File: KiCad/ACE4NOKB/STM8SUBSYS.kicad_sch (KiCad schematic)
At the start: 6 parts, among them J400 614008235023, J402 Conn_02x05_Odd_Even, J403 STLink2, J408 Conn_02x05_Odd_Even

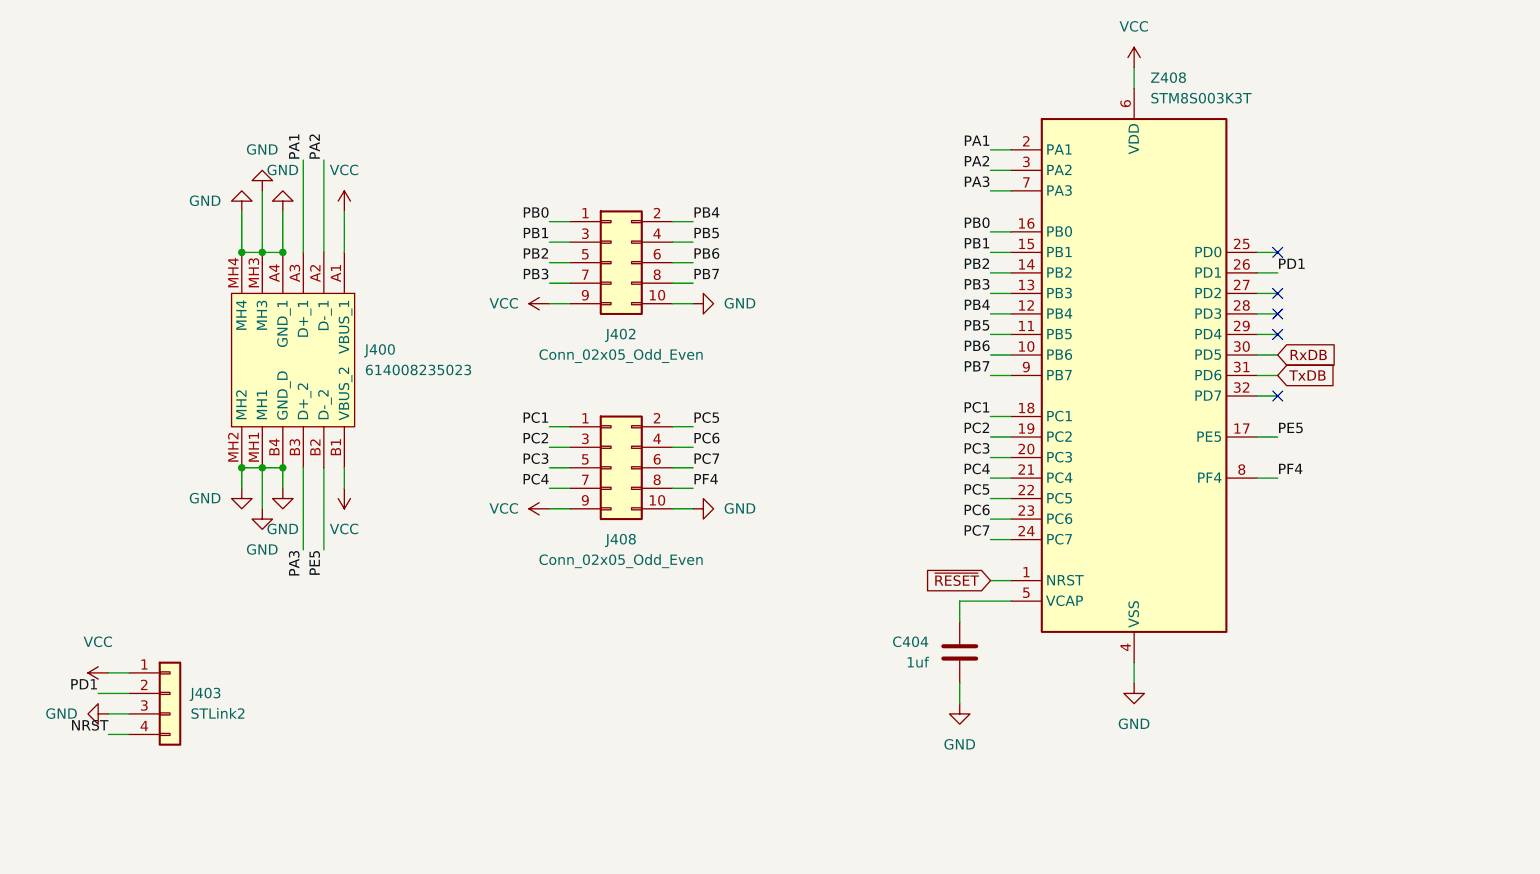
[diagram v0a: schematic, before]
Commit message: Fix mistake with ROM Select.
Signed-off-by: John Bradley <flypie@rocketmail.com>
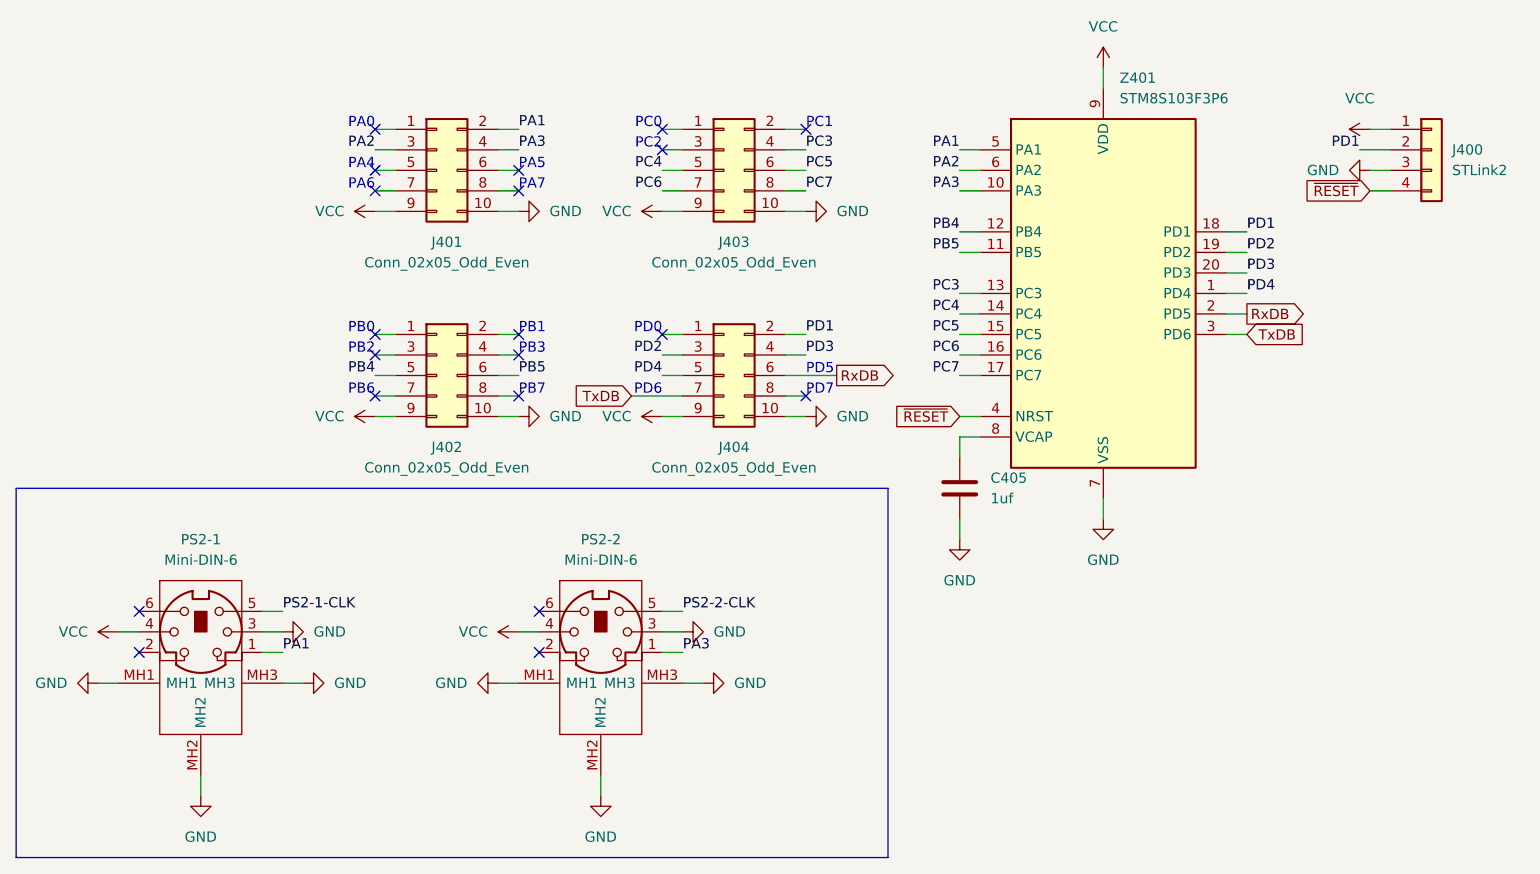
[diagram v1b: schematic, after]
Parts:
- removed C404: 1uf, Capacitor_THT:C_Disc_D3.0mm_W1.6mm_P2.50mm, symbol Device:C
- removed J400: 614008235023, 614008235023, symbol ExtraSymbols:614008235023
- removed J403: STLink2, Connector_PinHeader_2.54mm:PinHeader_1x04_P2.54mm_Vertical, symbol Connector_Generic:Conn_01x04
- removed J408: Conn_02x05_Odd_Even, Connector_PinHeader_2.54mm:PinHeader_2x05_P2.54mm_Vertical, symbol Connector_Generic:Conn_02x05_Odd_Even
- removed Z408: STM8S003K3T, Package_QFP:LQFP-32_7x7mm_P0.8mm, symbol MCU_ST_STM8:STM8S003K3T
- added C405: 1uf, Capacitor_THT:C_Disc_D3.0mm_W1.6mm_P2.50mm, symbol Device:C
- added J400: STLink2, Connector_PinHeader_2.54mm:PinHeader_1x04_P2.54mm_Vertical, symbol Connector_Generic:Conn_01x04
- added J401, J403, J404: Conn_02x05_Odd_Even, Connector_PinHeader_2.54mm:PinHeader_2x05_P2.54mm_Vertical, symbol Connector_Generic:Conn_02x05_Odd_Even
- added PS2-1, PS2-2: Mini-DIN-6, 57492661, symbol ExtraSymbols:5749266-1
- added Z401: STM8S103F3P6, Package_SO:TSSOP-20_4.4x6.5mm_P0.65mm, symbol MCU_ST_STM8:STM8S003F3P
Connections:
- net PB2 is gone; now on net PB4: J402.5 (Pin_5)
- net PB6 is gone; now on net PB5: J402.6 (Pin_6)
- net GND: now also C405.2, J400.3 (Pin_3), J401.10 (Pin_10), J403.10 (Pin_10), J404.10 (Pin_10), PS2-1.3, PS2-1.MH1, PS2-1.MH2, PS2-1.MH3, PS2-2.3, PS2-2.MH1, PS2-2.MH2, PS2-2.MH3, Z401.7 (VSS)
- net PA1: now also J401.2 (Pin_2), PS2-1.1, Z401.5 (PA1)
- net PA2: now also J401.3 (Pin_3), Z401.6 (PA2)
- net PA3: now also J401.4 (Pin_4), PS2-2.1, Z401.10 (PA3)
- net PB4: now also Z401.12 (PB4); no longer J402.2 (Pin_2)
- net PB5: now also Z401.11 (PB5); no longer J402.4 (Pin_4)
- net PC3: now also J403.4 (Pin_4), Z401.13 (PC3)
- net PC4: now also J403.5 (Pin_5), Z401.14 (PC4)
- net PC5: now also J403.6 (Pin_6), Z401.15 (PC5)
- net PC6: now also J403.7 (Pin_7), Z401.16 (PC6)
- net PC7: now also J403.8 (Pin_8), Z401.17 (PC7)
- net PD1: now also J400.2 (Pin_2), J404.2 (Pin_2), Z401.18 (PD1)
- net RxDB: now also J404.6 (Pin_6), Z401.2 (PD5)
- net TxDB: now also J404.7 (Pin_7), Z401.3 (PD6)
- net VCC: now also J400.1 (Pin_1), J401.9 (Pin_9), J403.9 (Pin_9), J404.9 (Pin_9), PS2-1.4, PS2-2.4, Z401.9 (VDD)
- net ~{RESET}: now also J400.4 (Pin_4), Z401.4 (NRST)
- net PB0: no longer names the net of J402.1 (Pin_1)
- net PB1: no longer names the net of J402.3 (Pin_3)
- net PB3: no longer names the net of J402.7 (Pin_7)
- net PB7: no longer names the net of J402.8 (Pin_8)
- new net: C405.1, Z401.8 (VCAP)
- new net PD2: J404.3 (Pin_3), Z401.19 (PD2)
- new net PD3: J404.4 (Pin_4), Z401.20 (PD3)
- new net PD4: J404.5 (Pin_5), Z401.1 (PD4)
- new net PS2-1-CLK: PS2-1.5
- new net PS2-2-CLK: PS2-2.5
- no-connect marks 5 -> 20
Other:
- note added: "PA0"
- note added: "PA4"
- note added: "PA5"
- note added: "PA6"
- note added: "PA7"
- note added: "PB0"
- note added: "PB1"
- note added: "PB2"
- note added: "PB3"
- note added: "PB6"
- note added: "PB7"
- note added: "PC0"
- note added: "PC1"
- note added: "PC2"
- note added: "PD0"
- note added: "PD5"
- note added: "PD6"
- note added: "PD7"
- title: ACE4NOKB -> JupiterAce Z80 plus KIO and new memory format.

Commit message: Update to last expermintal version. Uses clock sythsiser and can be switched between full ACE compatible and inhanced IO. Should be able to switch between multiple ROM images tosred on the same chip.
Signed-off-by: John Bradley <flypie@rocketmail.com>
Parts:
- C405: Manufacturer_Name Lelon -> (none); Manufacturer_Part_Number REA010M2CBK-0511P -> (none)
- J400: Manufacturer_Name Samtec -> (none); Manufacturer_Part_Number HTSW-104-24-F-S -> (none)
- J401, J402, J403, J404: Manufacturer_Name Amphenol FCI -> (none); Manufacturer_Part_Number 10129381-910001BLF -> (none)
- Z401: Manufacturer_Name STMicroelectronics -> (none); Manufacturer_Part_Number STM8S003K3T6CTR -> (none)

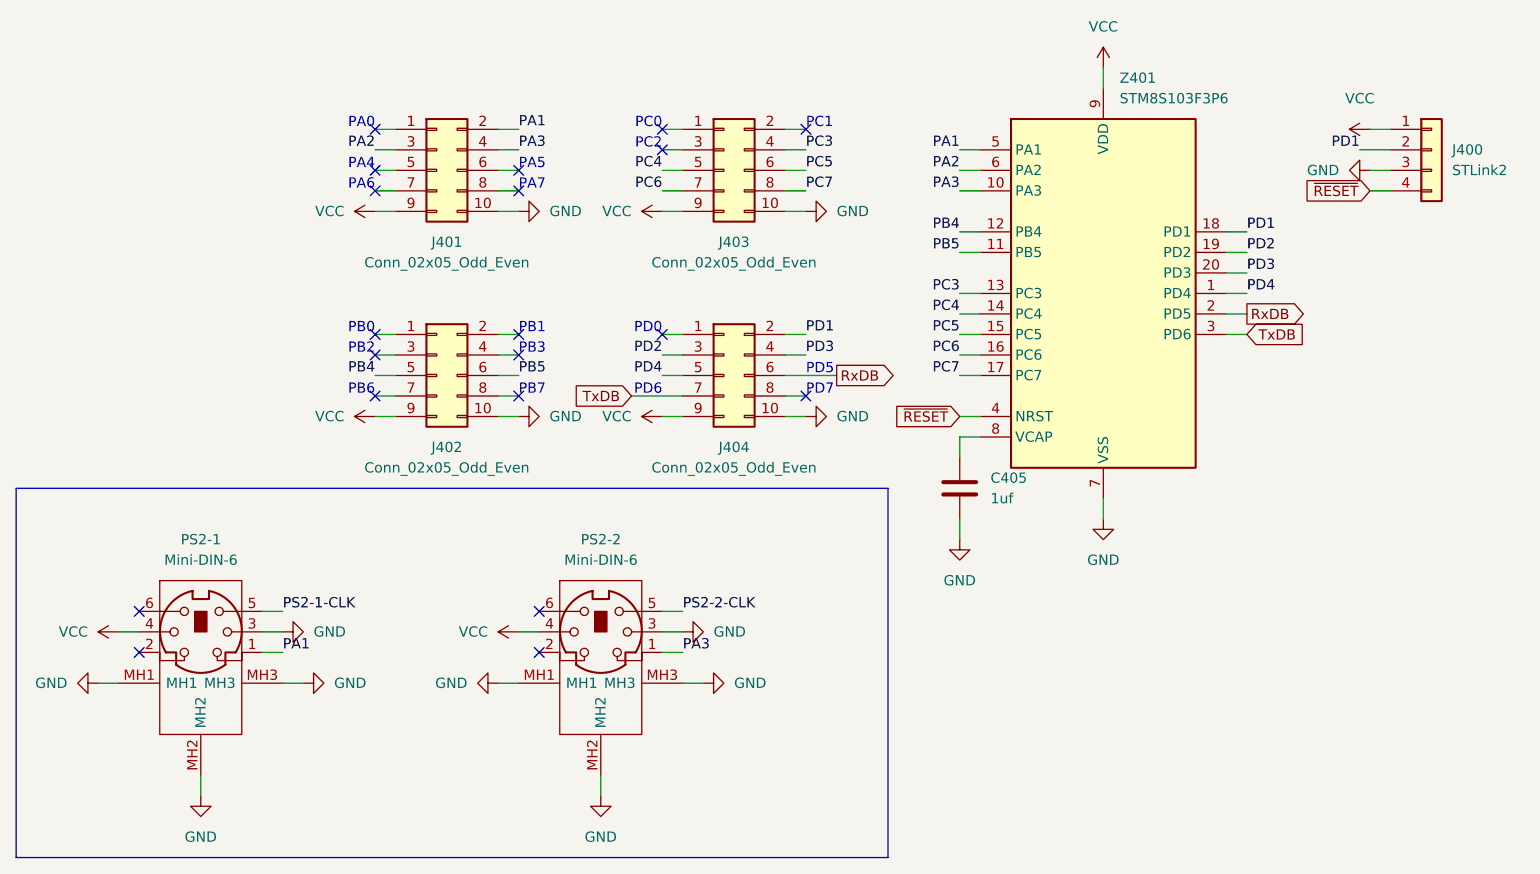
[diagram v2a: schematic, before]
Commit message: Version with KIO replaced with Z84C15 and Video and Character RAM as MultiPorted.
Signed-off-by: John Bradley <flypie@rocketmail.com>
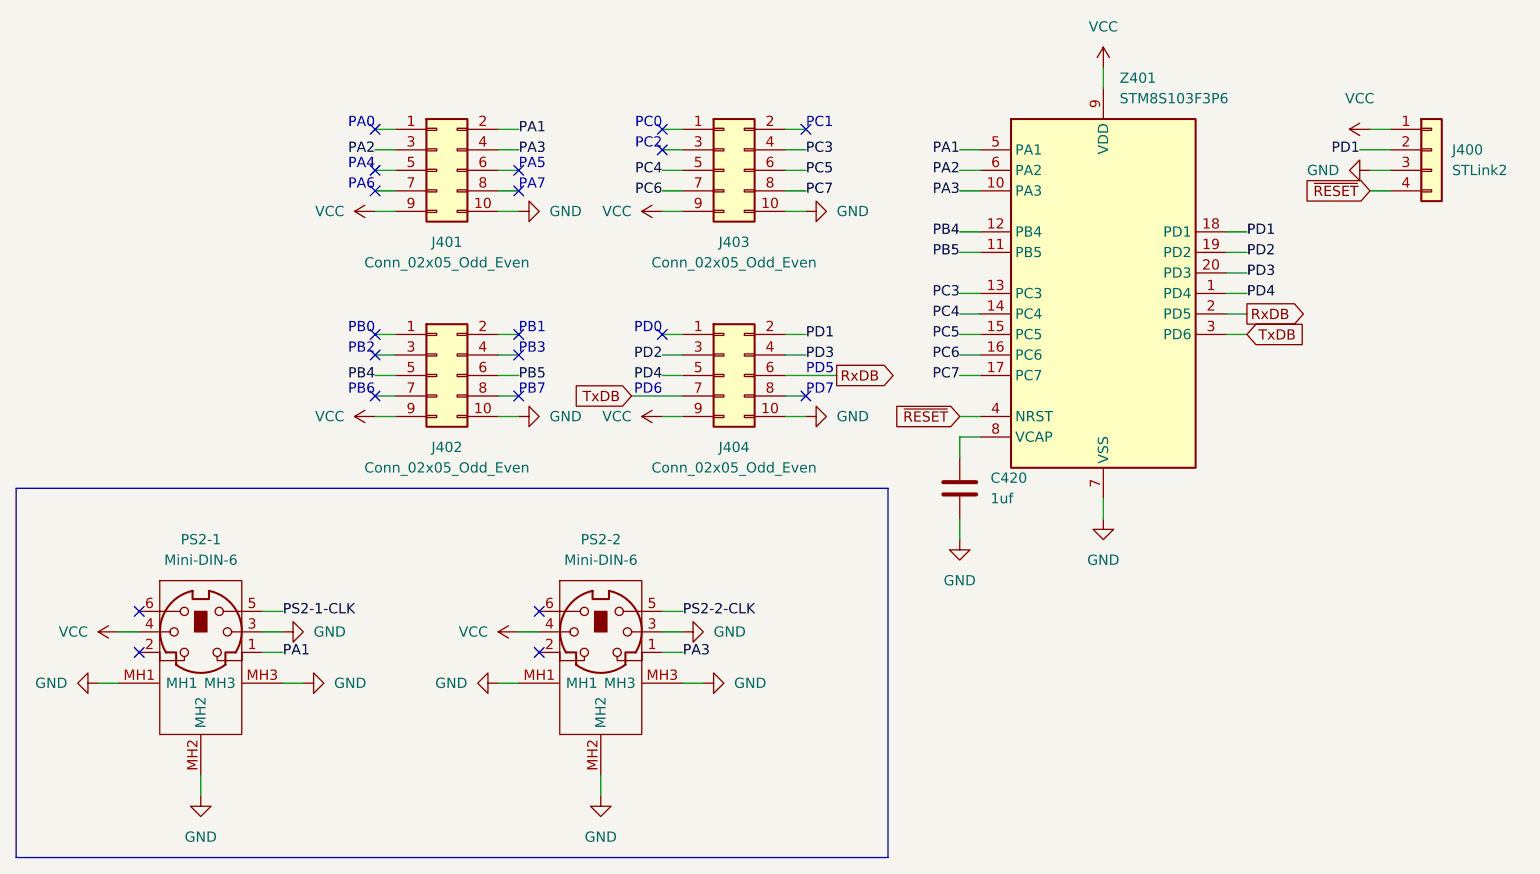
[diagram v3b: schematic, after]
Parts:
- renumbered C405 to C420
